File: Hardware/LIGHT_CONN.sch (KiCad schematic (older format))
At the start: 54 parts, among them U22 PCA9685BS

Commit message: Annotated schematic
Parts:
- gave numbers to parts that had none: 37
- renumbered R123 to R111, R124 to R112, R125 to R113, R126 to R114, R127 to R115, R128 to R116, R129 to R117, R130 to R118, R131 to R119, R132 to R120, R133 to R121, R134 to R122, R135 to R123, R136 to R124, R137 to R125, R138 to R126
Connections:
- wire segments 135 -> 129

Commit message: Fixing schematic issues
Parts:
- removed P28: CONN_01X01, symbol CONN_01X01
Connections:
- net MCU_GPIO_X_10/PWM_1 renamed MCU_GPIO_X_10/PWM2
- net MCU_GPIO_X_11/PWM_2 renamed MCU_GPIO_X_11/PWM3
- net MCU_GPIO_X_12/PWM_3 renamed MCU_GPIO_X_12/PWM4
- net MCU_GPIO_X_9 renamed MCU_GPIO_X_9/PWM1
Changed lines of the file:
@@
 $EndComp
 $Comp
-L GND-RESCUE-museV2-RESCUE-museV2 #PWR135
+L GND-RESCUE-museV2-RESCUE-museV2 #PWR0117
 U 1 1 57E62373
 P 2450 3150
-F 0 "#PWR135" H 2450 2900 50  0001 C CNN
+F 0 "#PWR0117" H 2450 2900 50  0001 C CNN
 F 1 "GND" H 2450 3000 50  0000 C CNN
 F 2 "" H 2450 3150 50  0000 C CNN
@@
 $EndComp
 $Comp
-L +3.3V-RESCUE-museV2 #PWR133
+L +3.3V-RESCUE-museV2 #PWR0118
 U 1 1 57E6273F
 P 2450 850
-F 0 "#PWR133" H 2450 700 50  0001 C CNN
+F 0 "#PWR0118" H 2450 700 50  0001 C CNN
 F 1 "+3.3V" H 2450 990 50  0000 C CNN
 F 2 "" H 2450 850 50  0000 C CNN
@@
 RGB LED Strip PWM Generator
 $Comp
-L +3.3V-RESCUE-museV2 #PWR132
+L +3.3V-RESCUE-museV2 #PWR0119
 U 1 1 57EA76FD
 P 1800 850
-F 0 "#PWR132" H 1800 700 50  0001 C CNN
+F 0 "#PWR0119" H 1800 700 50  0001 C CNN
 F 1 "+3.3V" H 1800 990 50  0000 C CNN
 F 2 "" H 1800 850 50  0000 C CNN
@@
 Connection ~ 1800 1250
 $Comp
-L GND-RESCUE-museV2-RESCUE-museV2 #PWR134
+L GND-RESCUE-museV2-RESCUE-museV2 #PWR0120
 U 1 1 57EF1660
 P 1800 3150
-F 0 "#PWR134" H 1800 2900 50  0001 C CNN
+F 0 "#PWR0120" H 1800 2900 50  0001 C CNN
 F 1 "GND" H 1800 3000 50  0000 C CNN
 F 2 "" H 1800 3150 50  0000 C CNN
@@
 $EndComp
 $Comp
-L +15VSB #PWR136
+L +15VSB #PWR0121
 U 1 1 57FFBADE
 P 3900 4100
-F 0 "#PWR136" H 3900 3950 50  0001 C CNN
+F 0 "#PWR0121" H 3900 3950 50  0001 C CNN
 F 1 "+15VSB" H 3900 4240 50  0000 C CNN
 F 2 "" H 3900 4100 50  0000 C CNN
@@
 	4650 4400 3900 4400
 $Comp
-L -15VSB #PWR137
+L -15VSB #PWR133
 U 1 1 57FFBC18
 P 3900 4400
-F 0 "#PWR137" H 3900 4500 50  0001 C CNN
+F 0 "#PWR133" H 3900 4500 50  0001 C CNN
 F 1 "-15VSB" H 3900 4550 50  0000 C CNN
 F 2 "" H 3900 4400 50  0000 C CNN
@@
 	4650 4950 3900 4950
 $Comp
-L +5V #PWR138
+L +5V #PWR0122
 U 1 1 57FFBF02
 P 3900 4650
-F 0 "#PWR138" H 3900 4500 50  0001 C CNN
+F 0 "#PWR0122" H 3900 4500 50  0001 C CNN
 F 1 "+5V" H 3900 4790 50  0000 C CNN
 F 2 "" H 3900 4650 50  0000 C CNN
@@
 $EndComp
 $Comp
-L +5VSB #PWR139
+L +5VSB #PWR0123
 U 1 1 57FFD044
 P 3900 4950
-F 0 "#PWR139" H 3900 5040 20  0001 C CNN
+F 0 "#PWR0123" H 3900 5040 20  0001 C CNN
 F 1 "+5VSB" H 3900 5100 55  0000 C CNN
 F 2 "" H 3900 4950 60  0000 C CNN
@@
 	4650 5250 3900 5250
 $Comp
-L +3.3V-RESCUE-museV2 #PWR140
+L +3.3V-RESCUE-museV2 #PWR0124
 U 1 1 57FFD630
 P 3900 5250
-F 0 "#PWR140" H 3900 5100 50  0001 C CNN
+F 0 "#PWR0124" H 3900 5100 50  0001 C CNN
 F 1 "+3.3V" H 3900 5390 50  0000 C CNN
 F 2 "" H 3900 5250 50  0000 C CNN
@@
 	4650 5550 3900 5550
 $Comp
-L +3.3VSB #PWR141
+L +3.3VSB #PWR0125
 U 1 1 57FFEA10
 P 3900 5550
-F 0 "#PWR141" H 3900 5510 30  0001 C CNN
+F 0 "#PWR0125" H 3900 5510 30  0001 C CNN
 F 1 "+3.3VSB" H 3900 5700 55  0000 C CNN
 F 2 "" H 3900 5550 60  0000 C CNN
@@
 	4650 5850 3900 5850
 $Comp
-L +1.8VSB #PWR142
+L +1.8VSB #PWR0126
 U 1 1 57FFEE42
 P 3900 5850
-F 0 "#PWR142" H 3900 5990 20  0001 C CNN
+F 0 "#PWR0126" H 3900 5990 20  0001 C CNN
 F 1 "+1.8VSB" H 3890 6000 55  0000 C CNN
 F 2 "" H 3900 5850 60  0000 C CNN
@@
 	4650 6150 3900 6150
 $Comp
-L GND-RESCUE-museV2-RESCUE-museV2 #PWR143
+L GND-RESCUE-museV2-RESCUE-museV2 #PWR0127
 U 1 1 57FFF105
 P 3900 6200
-F 0 "#PWR143" H 3900 5950 50  0001 C CNN
+F 0 "#PWR0127" H 3900 5950 50  0001 C CNN
 F 1 "GND" H 3900 6050 50  0000 C CNN
 F 2 "" H 3900 6200 50  0000 C CNN
@@
 Wire Wire Line
 	7350 5950 6800 5950
-Text GLabel 6800 5950 0    60   Input ~ 0
-MCU_GPIO_X_9
 $Comp
 L CONN_01X01 P24
@@
 Wire Wire Line
 	7350 6200 6800 6200
-Text GLabel 6800 6200 0    60   Input ~ 0
-MCU_GPIO_X_10/PWM_1
+Text GLabel 6800 5950 0    60   Input ~ 0
+MCU_GPIO_X_9/PWM1
 $Comp
 L CONN_01X01 P26
@@
 Wire Wire Line
 	7350 6700 6800 6700
-$Comp
-L CONN_01X01 P28
-U 1 1 58007CC4
-P 7550 6950
-F 0 "P28" H 7550 7050 50  0000 C CNN
-F 1 "CONN_01X01" V 7650 6950 50  0001 C CNN
-F 2 "" H 7550 6950 50  0000 C CNN
-F 3 "" H 7550 6950 50  0000 C CNN
-	1    7550 6950
-	1    0    0    -1
-$EndComp
-Wire Wire Line
-	7350 6950 6800 6950
+Text GLabel 6800 6200 0    60   Input ~ 0
+MCU_GPIO_X_10/PWM2
 Text GLabel 6800 6450 0    60   Input ~ 0
-MCU_GPIO_X_11/PWM_2
-Text GLabel 6800 6700 0    60   Input ~ 0
-MCU_GPIO_X_12/PWM_3
-Text GLabel 6800 6950 0    60   Input ~ 0
-MCU_GPIO_X_13/PWM_4
+MCU_GPIO_X_11/PWM3
 Wire Wire Line
 	4450 6750 4650 6750
@@
 Text Notes 3750 7550 0    60   ~ 0
 PWM Generator Breakouts
-Text GLabel 4200 7750 0    60   Input ~ 0
-PWM_X_1
 $Comp
 L CONN_01X01 P37
@@
 $EndComp
 Wire Wire Line
-	4650 8000 4200 8000
-Wire Wire Line
-	4200 8250 4650 8250
-Wire Wire Line
-	4200 7750 4650 7750
+	3850 8000 4650 8000
+Wire Wire Line
+	3850 8250 4650 8250
+Wire Wire Line
+	3850 7750 4650 7750
 $Comp
 L CONN_01X01 P40
@@
 $EndComp
 Wire Wire Line
-	4200 8500 4650 8500
-Text GLabel 4200 8000 0    60   Input ~ 0
+	3850 8500 4650 8500
+Text Label 3850 7750 0    60   ~ 0
+PWM_X_1
+Text Label 3850 8000 0    60   ~ 0
 PWM_X_2
-Text GLabel 4200 8250 0    60   Input ~ 0
+Text Label 3850 8250 0    60   ~ 0
 PWM_X_3
-Text GLabel 4200 8500 0    60   Input ~ 0
+Text Label 3850 8500 0    60   ~ 0
 PWM_X_4
+Text GLabel 6800 6700 0    60   Input ~ 0
+MCU_GPIO_X_12/PWM4
 $EndSCHEMATC

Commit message: Fixed schematic errors, added muse-v2-lib
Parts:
- removed P12, P17, P24, P25, P26: CONN_01X01, symbol CONN_01X01
- P10: value CONN_01X01 -> -15V; footprint (none) -> Pin_Headers:Pin_Header_Straight_1x01
- P11: value CONN_01X01 -> ~3; footprint (none) -> Pin_Headers:Pin_Header_Straight_1x01
- P13: value CONN_01X01 -> ~4; footprint (none) -> Pin_Headers:Pin_Header_Straight_1x01
- P14: value CONN_01X01 -> +5V; footprint (none) -> Pin_Headers:Pin_Header_Straight_1x01
- P15: value CONN_01X01 -> 5; footprint (none) -> Pin_Headers:Pin_Header_Straight_1x01
- P16: value CONN_01X01 -> 6; footprint (none) -> Pin_Headers:Pin_Header_Straight_1x01
- P18: value CONN_01X01 -> RX7; footprint (none) -> Pin_Headers:Pin_Header_Straight_1x01
- P19: value CONN_01X01 -> 3.3V; footprint (none) -> Pin_Headers:Pin_Header_Straight_1x01
- P20: value CONN_01X01 -> TX8; footprint (none) -> Pin_Headers:Pin_Header_Straight_1x01
- P21: value CONN_01X01 -> 1.8V; footprint (none) -> Pin_Headers:Pin_Header_Straight_1x01
- P22: value CONN_01X01 -> PSU_CTL; footprint (none) -> Pin_Headers:Pin_Header_Straight_1x01
- P23: value CONN_01X01 -> GND; footprint (none) -> Pin_Headers:Pin_Header_Straight_1x01
- P27: value CONN_01X01 -> D1; footprint (none) -> Pin_Headers:Pin_Header_Straight_1x01
- P29: value CONN_01X01 -> D2; footprint (none) -> Pin_Headers:Pin_Header_Straight_1x01
- P30: value CONN_01X01 -> D3; footprint (none) -> Pin_Headers:Pin_Header_Straight_1x01
- P31: value CONN_01X01 -> P1; footprint (none) -> Pin_Headers:Pin_Header_Straight_1x01
- P32: value CONN_01X01 -> L1.8_1; footprint (none) -> Pin_Headers:Pin_Header_Straight_1x01
- P33: value CONN_01X01 -> L3.3_1; footprint (none) -> Pin_Headers:Pin_Header_Straight_1x01
- P34: value CONN_01X01 -> P2; footprint (none) -> Pin_Headers:Pin_Header_Straight_1x01
- P35: value CONN_01X01 -> L1.8_2; footprint (none) -> Pin_Headers:Pin_Header_Straight_1x01
- P36: value CONN_01X01 -> L3.3_2; footprint (none) -> Pin_Headers:Pin_Header_Straight_1x01
- P37: value CONN_01X01 -> P3; footprint (none) -> Pin_Headers:Pin_Header_Straight_1x01
- P38: value CONN_01X01 -> L1.8_3; footprint (none) -> Pin_Headers:Pin_Header_Straight_1x01
- P39: value CONN_01X01 -> L3.3_3; footprint (none) -> Pin_Headers:Pin_Header_Straight_1x01
- P40: value CONN_01X01 -> P4; footprint (none) -> Pin_Headers:Pin_Header_Straight_1x01
- P41: value CONN_01X01 -> L1.8_4; footprint (none) -> Pin_Headers:Pin_Header_Straight_1x01
- P42: value CONN_01X01 -> L3.3_4; footprint (none) -> Pin_Headers:Pin_Header_Straight_1x01
- P6: footprint (none) -> Pin_Headers:Pin_Header_Straight_2x14
- P7: value CONN_01X01 -> ~1; footprint (none) -> Pin_Headers:Pin_Header_Straight_1x01
- P8: value CONN_01X01 -> +15V; footprint (none) -> Pin_Headers:Pin_Header_Straight_1x01
- P9: value CONN_01X01 -> ~2; footprint (none) -> Pin_Headers:Pin_Header_Straight_1x01
- R111, R112, R113, R114, R115, R116, R117, R118, R119, R120, R121, R122, R123, R124, R125, R126: footprint (none) -> Resistors_SMD:R_0402
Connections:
- net MCU_GPIO_X_1 renamed MCU_GPIO_X_1/PWM_X_1
- net MCU_GPIO_X_2 renamed MCU_GPIO_X_2/PWM_X_2
- net MCU_GPIO_X_3/UART_RX renamed MCU_GPIO_X_3/PWM_X_3
- net MCU_GPIO_X_4/UART_TX renamed MCU_GPIO_X_4/PWM_X_4
- net MCU_GPIO_X_7 renamed MCU_GPIO_X_7/UART_RX
- net MCU_GPIO_X_8 renamed MCU_GPIO_X_8/UART_TX
- net MCU_GPIO_X_9/PWM1 renamed PSU_CTL
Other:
- moved on the sheet: P14, P19, P21, P23

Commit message: Added proper audio connectors to schematic
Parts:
- U22: footprint (none) -> Housings_DFN_QFN:QFN-28-1EP_6x6mm_Pitch0.65mm
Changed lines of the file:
@@
 F 0 "U22" H 2150 1200 60  0000 C CNN
 F 1 "PCA9685BS" H 2750 -600 60  0000 C CNN
-F 2 "" H 3000 650 60  0001 C CNN
+F 2 "Housings_DFN_QFN:QFN-28-1EP_6x6mm_Pitch0.65mm" H 3000 650 60  0001 C CNN
 F 3 "" H 3000 650 60  0001 C CNN
 	1    2100 1150
@@
 $EndComp
 $Comp
-L GND-RESCUE-museV2-RESCUE-museV2 #PWR129
+L GND-RESCUE-museV2-RESCUE-museV2 #PWR0118
 U 1 1 57E62373
 P 2450 3150
-F 0 "#PWR129" H 2450 2900 50  0001 C CNN
+F 0 "#PWR0118" H 2450 2900 50  0001 C CNN
 F 1 "GND" H 2450 3000 50  0000 C CNN
 F 2 "" H 2450 3150 50  0000 C CNN
@@
 $EndComp
 $Comp
-L +3.3V-RESCUE-museV2 #PWR127
+L +3.3V-RESCUE-museV2 #PWR0119
 U 1 1 57E6273F
 P 2450 850
-F 0 "#PWR127" H 2450 700 50  0001 C CNN
+F 0 "#PWR0119" H 2450 700 50  0001 C CNN
 F 1 "+3.3V" H 2450 990 50  0000 C CNN
 F 2 "" H 2450 850 50  0000 C CNN
@@
 RGB LED Strip PWM Generator
 $Comp
-L +3.3V-RESCUE-museV2 #PWR126
+L +3.3V-RESCUE-museV2 #PWR0120
 U 1 1 57EA76FD
 P 1800 850
-F 0 "#PWR126" H 1800 700 50  0001 C CNN
+F 0 "#PWR0120" H 1800 700 50  0001 C CNN
 F 1 "+3.3V" H 1800 990 50  0000 C CNN
 F 2 "" H 1800 850 50  0000 C CNN
@@
 Connection ~ 1800 1250
 $Comp
-L GND-RESCUE-museV2-RESCUE-museV2 #PWR128
+L GND-RESCUE-museV2-RESCUE-museV2 #PWR0121
 U 1 1 57EF1660
 P 1800 3150
-F 0 "#PWR128" H 1800 2900 50  0001 C CNN
+F 0 "#PWR0121" H 1800 2900 50  0001 C CNN
 F 1 "GND" H 1800 3000 50  0000 C CNN
 F 2 "" H 1800 3150 50  0000 C CNN
@@
 $EndComp
 $Comp
-L +15VSB #PWR130
+L +15VSB #PWR0122
 U 1 1 57FFBADE
 P 3900 4100
-F 0 "#PWR130" H 3900 3950 50  0001 C CNN
+F 0 "#PWR0122" H 3900 3950 50  0001 C CNN
 F 1 "+15VSB" H 3900 4240 50  0000 C CNN
 F 2 "" H 3900 4100 50  0000 C CNN
@@
 	4650 4700 3900 4700
 $Comp
-L +5VSB #PWR132
+L +5VSB #PWR0123
 U 1 1 57FFD044
 P 3900 4700
-F 0 "#PWR132" H 3900 4790 20  0001 C CNN
+F 0 "#PWR0123" H 3900 4790 20  0001 C CNN
 F 1 "+5VSB" H 3900 4850 55  0000 C CNN
 F 2 "" H 3900 4700 60  0000 C CNN
@@
 	4650 5050 3900 5050
 $Comp
-L +3.3VSB #PWR133
+L +3.3VSB #PWR0124
 U 1 1 57FFEA10
 P 3900 5050
-F 0 "#PWR133" H 3900 5010 30  0001 C CNN
+F 0 "#PWR0124" H 3900 5010 30  0001 C CNN
 F 1 "+3.3VSB" H 3900 5200 55  0000 C CNN
 F 2 "" H 3900 5050 60  0000 C CNN
@@
 	4650 5350 3900 5350
 $Comp
-L +1.8VSB #PWR134
+L +1.8VSB #PWR0125
 U 1 1 57FFEE42
 P 3900 5350
-F 0 "#PWR134" H 3900 5490 20  0001 C CNN
+F 0 "#PWR0125" H 3900 5490 20  0001 C CNN
 F 1 "+1.8VSB" H 3890 5500 55  0000 C CNN
 F 2 "" H 3900 5350 60  0000 C CNN
@@
 	4650 5650 3900 5650
 $Comp
-L GND-RESCUE-museV2-RESCUE-museV2 #PWR135
+L GND-RESCUE-museV2-RESCUE-museV2 #PWR0126
 U 1 1 57FFF105
 P 3900 5700
-F 0 "#PWR135" H 3900 5450 50  0001 C CNN
+F 0 "#PWR0126" H 3900 5450 50  0001 C CNN
 F 1 "GND" H 3900 5550 50  0000 C CNN
 F 2 "" H 3900 5700 50  0000 C CNN

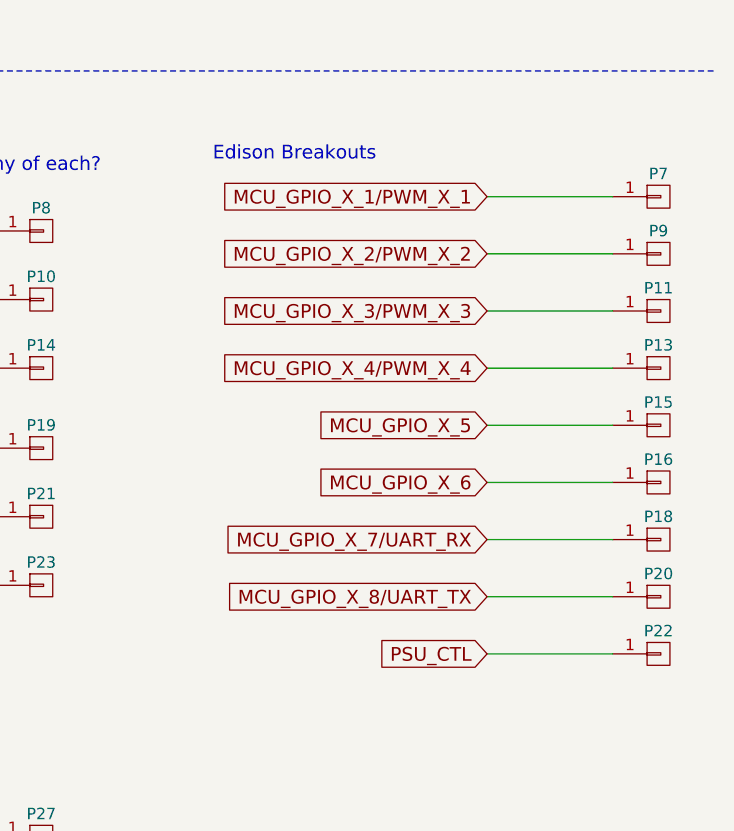
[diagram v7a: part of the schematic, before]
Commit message: Updated Edison pins for 3.5mm connections
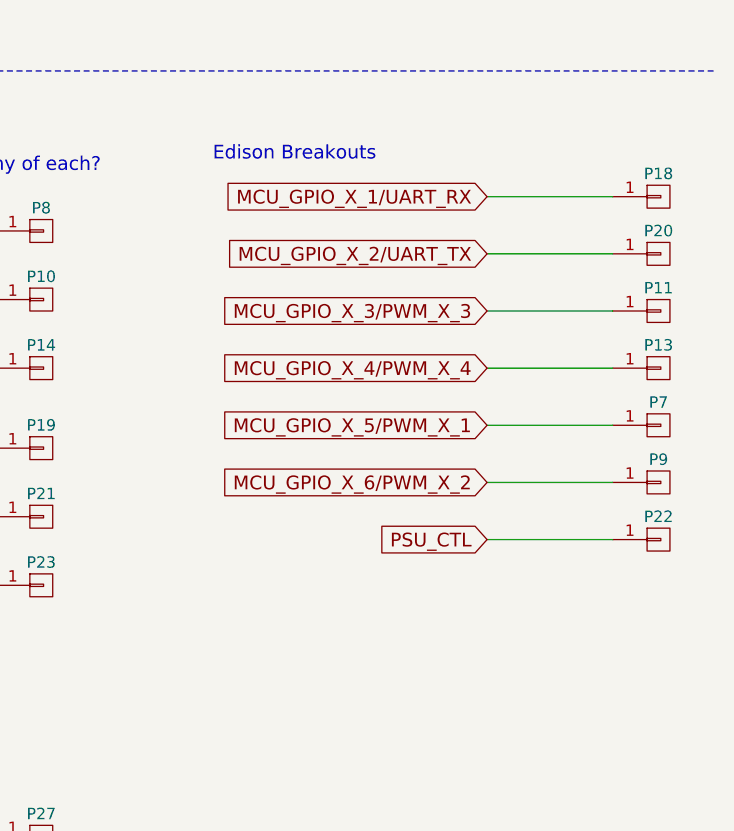
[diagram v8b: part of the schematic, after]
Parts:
- removed P15: 5, Pin_Headers:Pin_Header_Straight_1x01, symbol CONN_01X01
- removed P16: 6, Pin_Headers:Pin_Header_Straight_1x01, symbol CONN_01X01
- P18: value RX7 -> RX1
- P20: value TX8 -> TX2
- P7: value ~1 -> ~5
- P9: value ~2 -> ~6
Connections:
- net MCU_GPIO_X_1/PWM_X_1 renamed MCU_GPIO_X_5/PWM_X_1
- net MCU_GPIO_X_2/PWM_X_2 renamed MCU_GPIO_X_6/PWM_X_2
- net MCU_GPIO_X_7/UART_RX renamed MCU_GPIO_X_1/UART_RX
- net MCU_GPIO_X_8/UART_TX renamed MCU_GPIO_X_2/UART_TX
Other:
- moved on the sheet: P18, P20, P22, P7, P9
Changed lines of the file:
@@
 L CONN_01X01 P9
 U 1 1 58006FC7
-P 7550 4200
-F 0 "P9" H 7550 4300 50  0000 C CNN
-F 1 "~2" V 7650 4200 50  0001 C CNN
-F 2 "Pin_Headers:Pin_Header_Straight_1x01" H 7550 4200 50  0001 C CNN
-F 3 "" H 7550 4200 50  0000 C CNN
-	1    7550 4200
+P 7550 5200
+F 0 "P9" H 7550 5300 50  0000 C CNN
+F 1 "~6" V 7650 5200 50  0001 C CNN
+F 2 "Pin_Headers:Pin_Header_Straight_1x01" H 7550 5200 50  0001 C CNN
+F 3 "" H 7550 5200 50  0000 C CNN
+	1    7550 5200
 	1    0    0    -1
 $EndComp
@@
 L CONN_01X01 P7
 U 1 1 58006FCD
-P 7550 3950
-F 0 "P7" H 7550 4050 50  0000 C CNN
-F 1 "~1" V 7650 3950 50  0001 C CNN
-F 2 "Pin_Headers:Pin_Header_Straight_1x01" H 7550 3950 50  0001 C CNN
-F 3 "" H 7550 3950 50  0000 C CNN
-	1    7550 3950
-	1    0    0    -1
-$EndComp
-Wire Wire Line
-	6800 3950 7350 3950
-Wire Wire Line
-	7350 4200 6800 4200
+P 7550 4950
+F 0 "P7" H 7550 5050 50  0000 C CNN
+F 1 "~5" V 7650 4950 50  0001 C CNN
+F 2 "Pin_Headers:Pin_Header_Straight_1x01" H 7550 4950 50  0001 C CNN
+F 3 "" H 7550 4950 50  0000 C CNN
+	1    7550 4950
+	1    0    0    -1
+$EndComp
+Wire Wire Line
+	6800 4950 7350 4950
+Wire Wire Line
+	7350 5200 6800 5200
 Wire Wire Line
 	6800 4450 7350 4450
@@
 Text GLabel 6800 4700 0    60   Input ~ 0
 MCU_GPIO_X_4/PWM_X_4
-Text GLabel 6800 4950 0    60   Input ~ 0
-MCU_GPIO_X_5
-$Comp
-L CONN_01X01 P16
-U 1 1 58007781
-P 7550 5200
-F 0 "P16" H 7550 5300 50  0000 C CNN
-F 1 "6" V 7650 5200 50  0001 C CNN
-F 2 "Pin_Headers:Pin_Header_Straight_1x01" H 7550 5200 50  0001 C CNN
-F 3 "" H 7550 5200 50  0000 C CNN
-	1    7550 5200
-	1    0    0    -1
-$EndComp
-$Comp
-L CONN_01X01 P15
-U 1 1 58007787
-P 7550 4950
-F 0 "P15" H 7550 5050 50  0000 C CNN
-F 1 "5" V 7650 4950 50  0001 C CNN
-F 2 "Pin_Headers:Pin_Header_Straight_1x01" H 7550 4950 50  0001 C CNN
-F 3 "" H 7550 4950 50  0000 C CNN
-	1    7550 4950
-	1    0    0    -1
-$EndComp
-Wire Wire Line
-	6800 4950 7350 4950
-Wire Wire Line
-	7350 5200 6800 5200
-Text GLabel 6800 5200 0    60   Input ~ 0
-MCU_GPIO_X_6
-Text GLabel 6800 5450 0    60   Input ~ 0
-MCU_GPIO_X_7/UART_RX
+Text GLabel 6800 3950 0    60   Input ~ 0
+MCU_GPIO_X_1/UART_RX
 $Comp
 L CONN_01X01 P20
 U 1 1 58007A71
-P 7550 5700
-F 0 "P20" H 7550 5800 50  0000 C CNN
-F 1 "TX8" V 7650 5700 50  0001 C CNN
-F 2 "Pin_Headers:Pin_Header_Straight_1x01" H 7550 5700 50  0001 C CNN
-F 3 "" H 7550 5700 50  0000 C CNN
-	1    7550 5700
+P 7550 4200
+F 0 "P20" H 7550 4300 50  0000 C CNN
+F 1 "TX2" V 7650 4200 50  0001 C CNN
+F 2 "Pin_Headers:Pin_Header_Straight_1x01" H 7550 4200 50  0001 C CNN
+F 3 "" H 7550 4200 50  0000 C CNN
+	1    7550 4200
 	1    0    0    -1
 $EndComp
@@
 L CONN_01X01 P18
 U 1 1 58007A77
-P 7550 5450
-F 0 "P18" H 7550 5550 50  0000 C CNN
-F 1 "RX7" V 7650 5450 50  0001 C CNN
-F 2 "Pin_Headers:Pin_Header_Straight_1x01" H 7550 5450 50  0001 C CNN
-F 3 "" H 7550 5450 50  0000 C CNN
-	1    7550 5450
-	1    0    0    -1
-$EndComp
-Wire Wire Line
-	6800 5450 7350 5450
-Wire Wire Line
-	7350 5700 6800 5700
-Text GLabel 6800 5700 0    60   Input ~ 0
-MCU_GPIO_X_8/UART_TX
+P 7550 3950
+F 0 "P18" H 7550 4050 50  0000 C CNN
+F 1 "RX1" V 7650 3950 50  0001 C CNN
+F 2 "Pin_Headers:Pin_Header_Straight_1x01" H 7550 3950 50  0001 C CNN
+F 3 "" H 7550 3950 50  0000 C CNN
+	1    7550 3950
+	1    0    0    -1
+$EndComp
+Wire Wire Line
+	6800 3950 7350 3950
+Wire Wire Line
+	7350 4200 6800 4200
+Text GLabel 6800 4200 0    60   Input ~ 0
+MCU_GPIO_X_2/UART_TX
 Wire Wire Line
 	4450 6750 4650 6750
@@
 Text GLabel 6800 4450 0    60   Input ~ 0
 MCU_GPIO_X_3/PWM_X_3
-Text GLabel 6800 4200 0    60   Input ~ 0
-MCU_GPIO_X_2/PWM_X_2
-Text GLabel 6800 3950 0    60   Input ~ 0
-MCU_GPIO_X_1/PWM_X_1
+Text GLabel 6800 5200 0    60   Input ~ 0
+MCU_GPIO_X_6/PWM_X_2
+Text GLabel 6800 4950 0    60   Input ~ 0
+MCU_GPIO_X_5/PWM_X_1
 $Comp
 L CONN_01X01 P22
 U 1 1 585A0CF3
-P 7550 5950
-F 0 "P22" H 7550 6050 50  0000 C CNN
-F 1 "PSU_CTL" V 7650 5950 50  0001 C CNN
-F 2 "Pin_Headers:Pin_Header_Straight_1x01" H 7550 5950 50  0001 C CNN
-F 3 "" H 7550 5950 50  0000 C CNN
-	1    7550 5950
-	1    0    0    -1
-$EndComp
-Wire Wire Line
-	7350 5950 6800 5950
-Text GLabel 6800 5950 0    60   Input ~ 0
+P 7550 5450
+F 0 "P22" H 7550 5550 50  0000 C CNN
+F 1 "PSU_CTL" V 7650 5450 50  0001 C CNN
+F 2 "Pin_Headers:Pin_Header_Straight_1x01" H 7550 5450 50  0001 C CNN
+F 3 "" H 7550 5450 50  0000 C CNN
+	1    7550 5450
+	1    0    0    -1
+$EndComp
+Wire Wire Line
+	7350 5450 6800 5450
+Text GLabel 6800 5450 0    60   Input ~ 0
 PSU_CTL
 $EndSCHEMATC
